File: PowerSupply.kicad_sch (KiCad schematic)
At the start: 20 parts, among them J2 Jumper, J3 LiPo 3,7V Batt., J4 Jumper, SW1 Switch_SP3T, U1 MCP73831, U2 XC9142B50C, U3 XC6220B33

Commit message: Renamed files.
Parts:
- J2, J4: symbol rp2040-launchpad-PCB:Jumper -> rp2350b-launchpad-PCB:Jumper
- SW1: symbol rp2040-launchpad-PCB:Switch_SP3T -> rp2350b-launchpad-PCB:Switch_SP3T
- U1: symbol rp2040-launchpad-PCB:MCP73831 -> rp2350b-launchpad-PCB:MCP73831
- U2: symbol rp2040-launchpad-PCB:XC9142B50C -> rp2350b-launchpad-PCB:XC9142B50C
- U3: symbol rp2040-launchpad-PCB:XC6220B33 -> rp2350b-launchpad-PCB:XC6220B33
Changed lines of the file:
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@@
 	)
 	(symbol
-		(lib_id "rp2040-launchpad-PCB:+5V_DBG")
+		(lib_id "rp2350b-launchpad-PCB:+5V_DBG")
 		(at 243.84 74.93 0)
 		(unit 1)
@@
 	)
 	(symbol
-		(lib_id "rp2040-launchpad-PCB:+3V3_DBG")
+		(lib_id "rp2350b-launchpad-PCB:+3V3_DBG")
 		(at 243.84 87.63 0)
 		(unit 1)
@@
 	)
 	(symbol
-		(lib_id "rp2040-launchpad-PCB:XC9142B50C")
+		(lib_id "rp2350b-launchpad-PCB:XC9142B50C")
 		(at 134.62 95.25 0)
 		(unit 1)
@@
 	)
 	(symbol
-		(lib_id "rp2040-launchpad-PCB:XC6220B33")
+		(lib_id "rp2350b-launchpad-PCB:XC6220B33")
 		(at 204.47 95.25 0)
 		(unit 1)
@@
 	)
 	(symbol
-		(lib_id "rp2040-launchpad-PCB:GND_DBG")
+		(lib_id "rp2350b-launchpad-PCB:GND_DBG")
 		(at 232.41 113.03 0)
 		(unit 1)
@@
 	)
 	(symbol
-		(lib_id "rp2040-launchpad-PCB:MCP73831")
+		(lib_id "rp2350b-launchpad-PCB:MCP73831")
 		(at 73.66 95.25 0)
 		(unit 1)
@@
 	)
 	(symbol
-		(lib_id "rp2040-launchpad-PCB:Jumper")
+		(lib_id "rp2350b-launchpad-PCB:Jumper")
 		(at 87.63 87.63 0)
 		(unit 1)
@@
 	)
 	(symbol
-		(lib_id "rp2040-launchpad-PCB:Switch_SP3T")
+		(lib_id "rp2350b-launchpad-PCB:Switch_SP3T")
 		(at 166.37 87.63 0)
 		(mirror y)
@@
 	)
 	(symbol
-		(lib_id "rp2040-launchpad-PCB:Jumper")
+		(lib_id "rp2350b-launchpad-PCB:Jumper")
 		(at 167.64 123.19 0)
 		(unit 1)
@@
 		)
 		(instances
-			(project "rp2040-launchpad-PCB"
+			(project "rp2350b-launchpad-PCB"
 				(path "/60290668-847e-40fe-8544-1cbbc26023b6/00000000-0000-0000-0000-00006284c5d3"
 					(reference "J4")

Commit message: More fixes...
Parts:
- J3: footprint rp2350-launchpad:JST-S2B-PH-KL -> rp2350b-launchpad-PCB:JST-S2B-PH-KL
- SW1: footprint rp2350-launchpad:PCM13SMTR -> rp2350b-launchpad-PCB:PCM13SMTR
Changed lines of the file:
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@@
 			)
 		)
-		(property "Footprint" "rp2350-launchpad:JST-S2B-PH-KL"
+		(property "Footprint" "rp2350b-launchpad-PCB:JST-S2B-PH-KL"
 			(at 93.98 100.33 0)
 			(effects
@@
 			)
 		)
-		(property "Footprint" "rp2350-launchpad:PCM13SMTR"
+		(property "Footprint" "rp2350b-launchpad-PCB:PCM13SMTR"
 			(at 166.37 87.63 0)
 			(effects

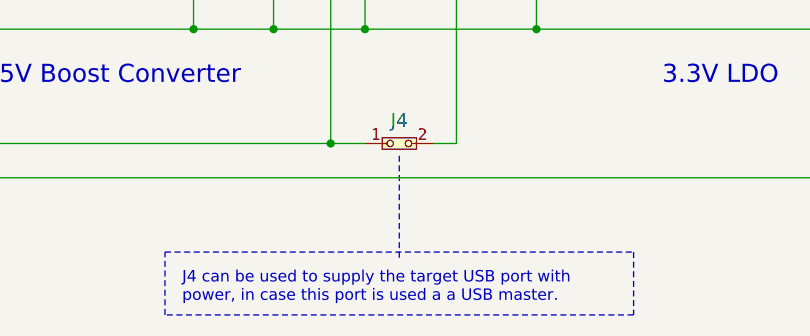
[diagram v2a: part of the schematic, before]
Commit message: Footprint cleanup.
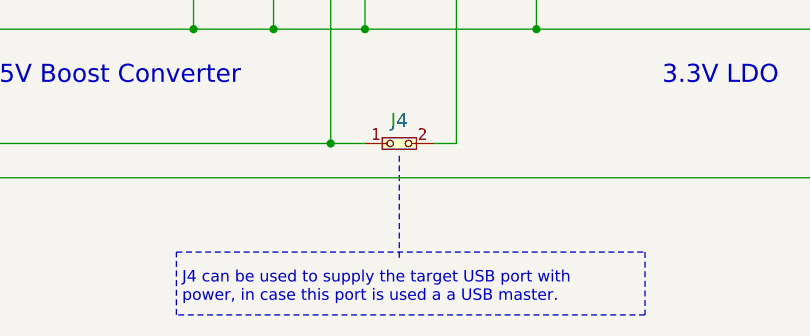
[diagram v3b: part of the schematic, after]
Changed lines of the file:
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@@
 	)
 	(rectangle
-		(start 141.605 135.255)
-		(end 193.675 142.24)
+		(start 142.875 135.255)
+		(end 194.945 142.24)
 		(stroke
 			(width 0)

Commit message: Ready for Version v1.0. Changed PCB to comply with RPi design 'rules'. Without using special components and PCB designs, the PCB may not be produced :\
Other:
- company: (none) -> ISS Intelligent Sensor Solutions
- title: (none) -> RP2350 Launchpad
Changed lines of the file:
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@@
 	(generator_version "8.0")
 	(paper "A4")
+	(title_block
+		(title "RP2350 Launchpad")
+		(date "2024-12-10")
+		(rev "v1.0")
+		(company "ISS Intelligent Sensor Solutions")
+		(comment 1 "(C) 2024 A. Terstegge")
+		(comment 2 "and integrated RP2040-based debugger")
+		(comment 3 "A TI-style Launchpad with RP2350 MCU")
+	)
 	(junction
 		(at 85.09 110.49)

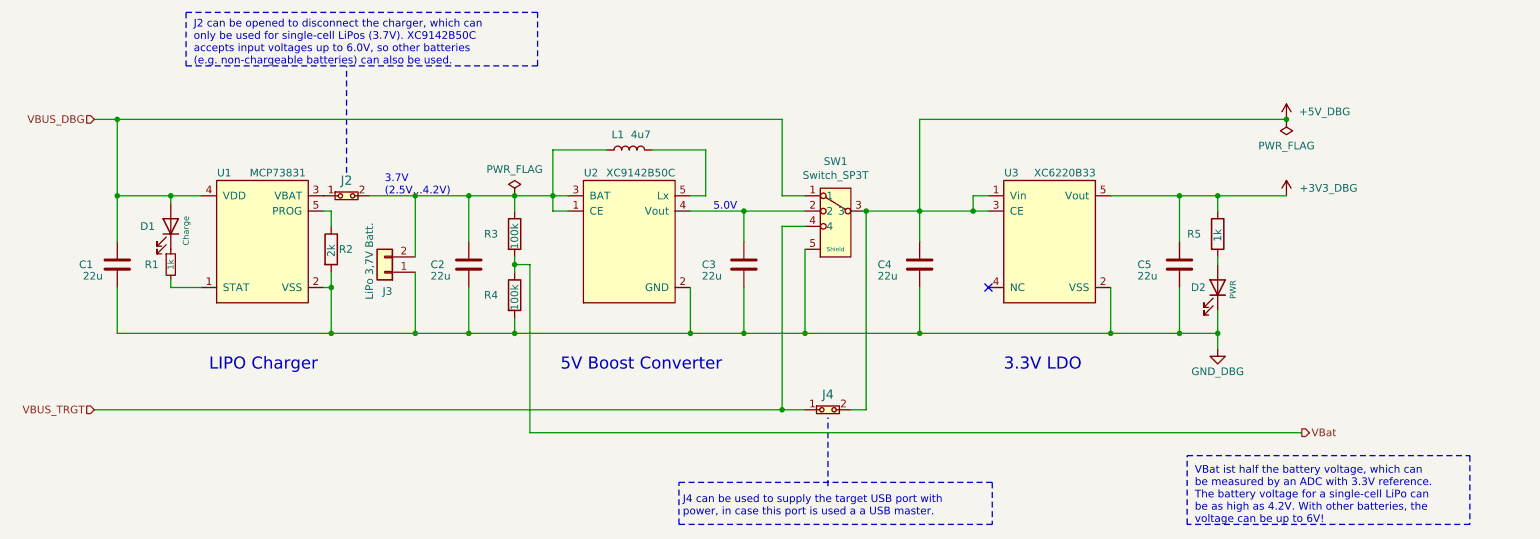
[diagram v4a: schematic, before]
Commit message: Updates for better JLCPCB processing. Version is now 1.1
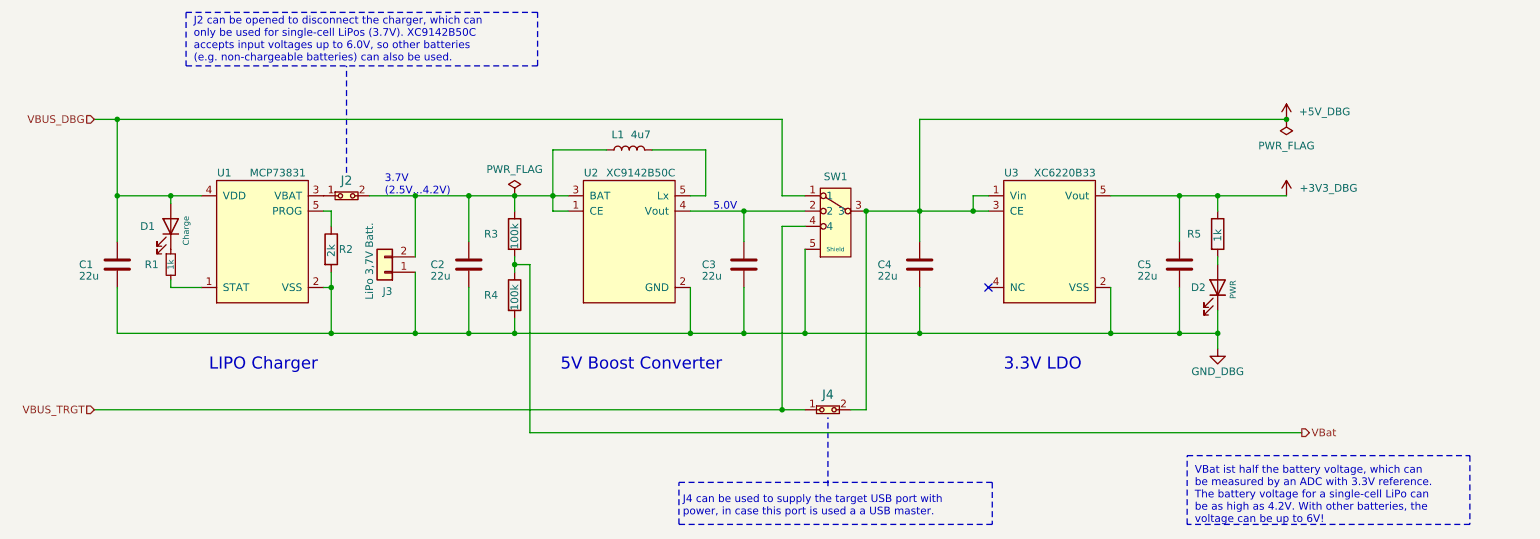
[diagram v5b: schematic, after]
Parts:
- C1, C2, C3, C4, C5: Hersteller (none) -> Samsung Electro-Mechanics; JLCPCB Part # (none) -> C45783; MANUFACTURER z.B. Kemet -> Samsung Electro-Mechanics
- D1, D2: Hersteller (none) -> Hubei KENTO Elec; JLCPCB Part # (none) -> C2290; STANDARD unkritisch -> (none)
- L1: footprint Inductor_SMD:L_1008_2520Metric -> rp2350b-launchpad-PCB:AOTA-B201610S3R3-101-T; Hersteller (none) -> Abracon LLC; JLCPCB Part # (none) -> C42411119; MANUFACTURER BOURNS -> Abracon LLC
- R1, R5: Hersteller (none) -> UNI-ROYAL(Uniroyal Elec); JLCPCB Part # (none) -> C21190
- R2: Hersteller (none) -> UNI-ROYAL(Uniroyal Elec); JLCPCB Part # (none) -> C22975; STANDARD 1% Toleranz -> (none)
- R3, R4: Hersteller (none) -> UNI-ROYAL(Uniroyal Elec); JLCPCB Part # (none) -> C25803; STANDARD unkritisch -> (none)
- SW1: value Switch_SP3T -> Power Select; Hersteller (none) -> C&K; JLCPCB Part # (none) -> C221842
- U1: Hersteller (none) -> Microchip Tech; JLCPCB Part # (none) -> C424093
- U2: Hersteller (none) -> Torex Semicon; JLCPCB Part # (none) -> C2468807
- U3: Hersteller (none) -> TDSEMIC; JLCPCB Part # (none) -> C22466451

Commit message: Ready for v1.1
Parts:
- J2: footprint Jumper:SolderJumper-2_P1.3mm_Bridged_RoundedPad1.0x1.5mm -> Jumper:SolderJumper-2_P1.3mm_Open_RoundedPad1.0x1.5mm
- R1, R5: value 1k -> 2k; JLCPCB Part # C21190 -> C22975
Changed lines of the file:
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@@
 			)
 		)
-		(property "Value" "1k"
+		(property "Value" "2k"
 			(at 58.42 99.06 90)
 			(effects
@@
 			)
 		)
-		(property "Datasheet" "https://jlcpcb.com/partdetail/21904-0603WAF1001T5E/C21190"
+		(property "Datasheet" "https://jlcpcb.com/partdetail/23702-0603WAF2001T5E/C22975"
 			(at 58.42 99.06 0)
 			(effects
@@
 			)
 		)
-		(property "JLCPCB Part #" "C21190"
+		(property "JLCPCB Part #" "C22975"
 			(at 58.42 99.06 0)
 			(effects
@@
 		(dnp no)
 		(property "Reference" "R5"
-			(at 227.33 93.98 0)
+			(at 227.965 93.98 0)
 			(effects
 				(font
@@
 			)
 		)
-		(property "Value" "1k"
+		(property "Value" "2k"
 			(at 232.41 95.25 90)
 			(effects
@@
 			)
 		)
-		(property "Datasheet" "https://jlcpcb.com/partdetail/21904-0603WAF1001T5E/C21190"
+		(property "Datasheet" "https://jlcpcb.com/partdetail/23702-0603WAF2001T5E/C22975"
 			(at 232.41 93.98 0)
 			(effects
@@
 			)
 		)
-		(property "JLCPCB Part #" "C21190"
+		(property "JLCPCB Part #" "C22975"
 			(at 232.41 93.98 0)
 			(effects
@@
 			)
 		)
-		(property "Footprint" "Jumper:SolderJumper-2_P1.3mm_Bridged_RoundedPad1.0x1.5mm"
+		(property "Footprint" "Jumper:SolderJumper-2_P1.3mm_Open_RoundedPad1.0x1.5mm"
 			(at 91.44 87.63 0)
 			(effects

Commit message: Last small fixes for v1.11
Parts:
- D1, D2: JLCPCB Part # C2290 -> C84269
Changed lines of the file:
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@@
 			)
 		)
-		(property "JLCPCB Part #" "C2290"
+		(property "JLCPCB Part #" "C84269"
 			(at 58.42 92.71 0)
 			(effects
@@
 			)
 		)
-		(property "JLCPCB Part #" "C2290"
+		(property "JLCPCB Part #" "C84269"
 			(at 232.41 102.87 0)
 			(effects
